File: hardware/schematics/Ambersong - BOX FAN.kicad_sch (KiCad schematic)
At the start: 35 parts

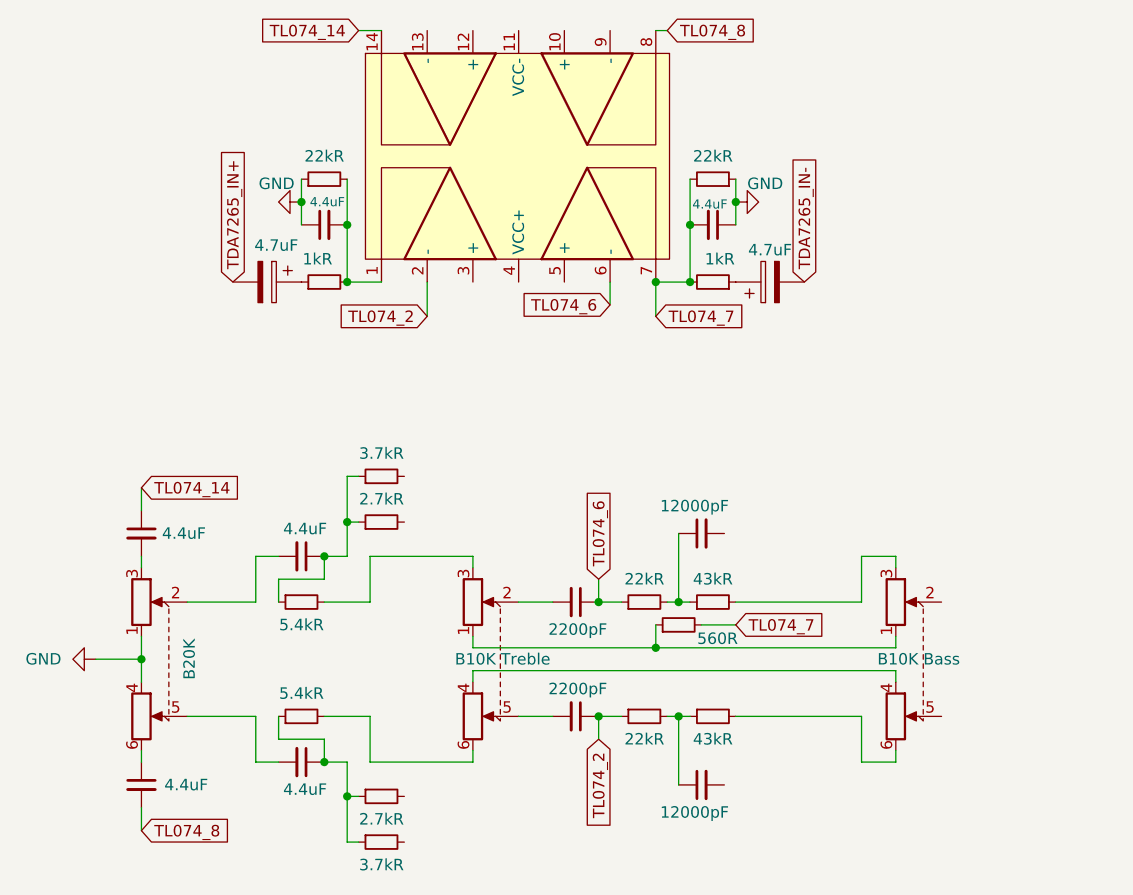
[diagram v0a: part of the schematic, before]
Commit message: First render, collated schematic PDF, the author's BOX FAN sheet edit; the running hare is carved out of the licences
The hare is all rights reserved; photos and renders are CC BY-NC-ND 4.0.
KiCad and SketchUp backups are ignored. NOTICE credits Claude Code and
Codex, as the README does.

Co-Authored-By: Claude Opus 5.5 (1M context) <noreply@anthropic.com>
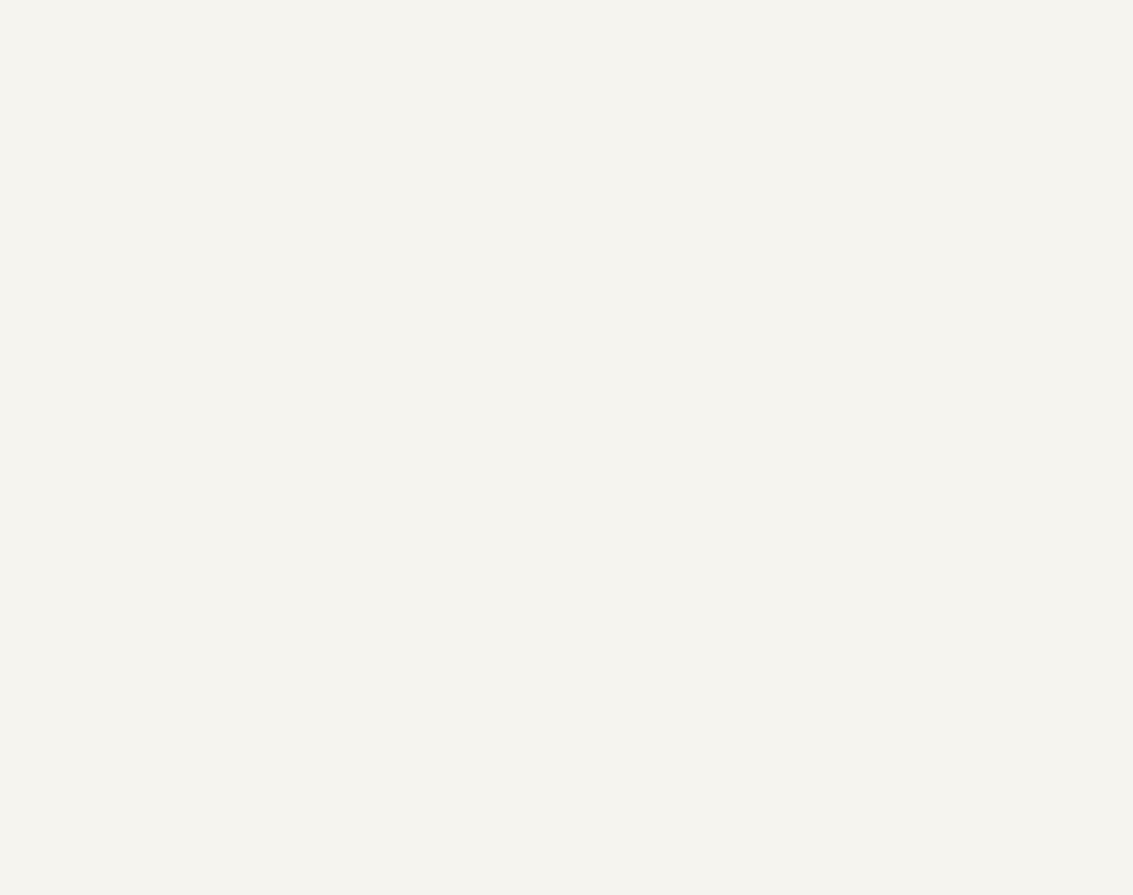
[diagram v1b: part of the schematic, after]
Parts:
- removed C1, C2, C3, C4, C5, C6: 4.4uF, symbol Device:C_Small
- removed C10, C12: 12000pF, symbol Device:C_Small
- removed C11, C9: 2200pF, symbol Device:C_Small
- removed C7, C8: 4.7uF, symbol Device:C_Polarized
- removed R10, R5, R6, R8: 22kR, symbol Device:R_Small
- removed R11, R9: 43kR, symbol Device:R_Small
- removed R12: 560R, symbol Device:R_Small
- removed R13, R16: 2.7kR, symbol Device:R_Small
- removed R14, R15: 3.7kR, symbol Device:R_Small
- removed R2, R3: 5.4kR, symbol Device:R_Small
- removed R4, R7: 1kR, symbol Device:R_Small
- removed RV1: B20K, symbol Device:R_Potentiometer_Dual
- removed RV2: B10K Treble, symbol Device:R_Potentiometer_Dual
- removed RV3: B10K Bass, symbol Device:R_Potentiometer_Dual
- removed U41: ~, symbol Mine:TL074C
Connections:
- net GND renamed 20V_GND
